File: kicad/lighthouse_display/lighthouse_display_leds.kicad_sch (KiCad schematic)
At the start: 99 parts

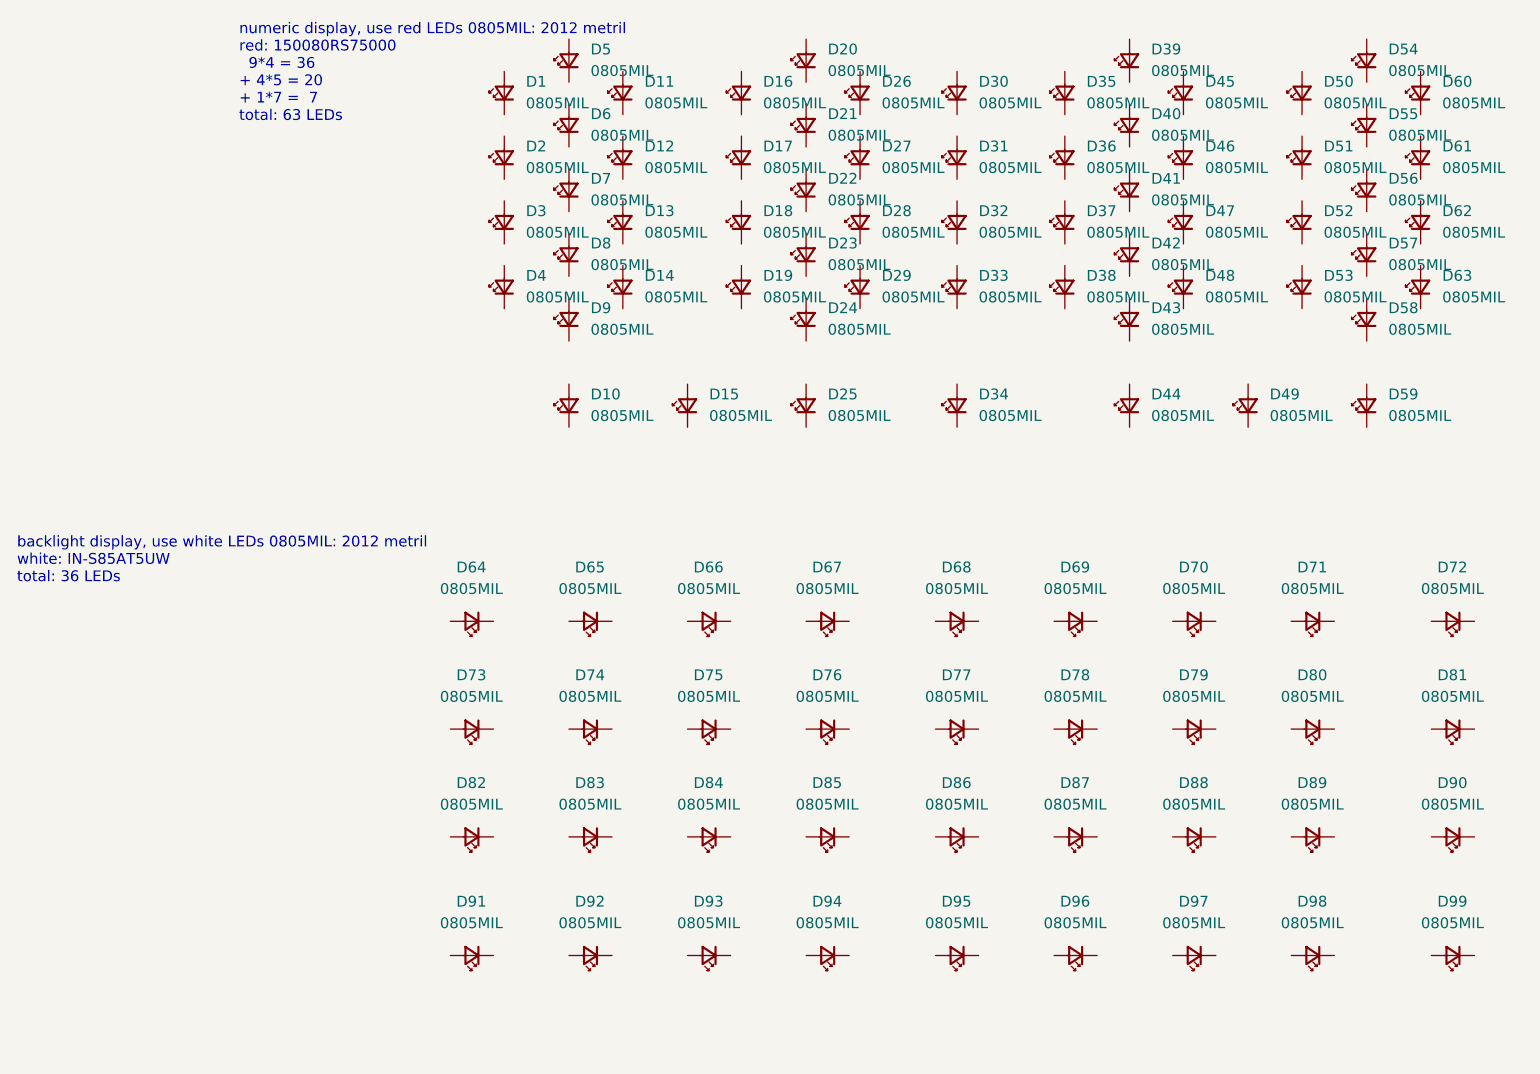
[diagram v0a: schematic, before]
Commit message: white LED driver TPS61176RTER added in lib and sch
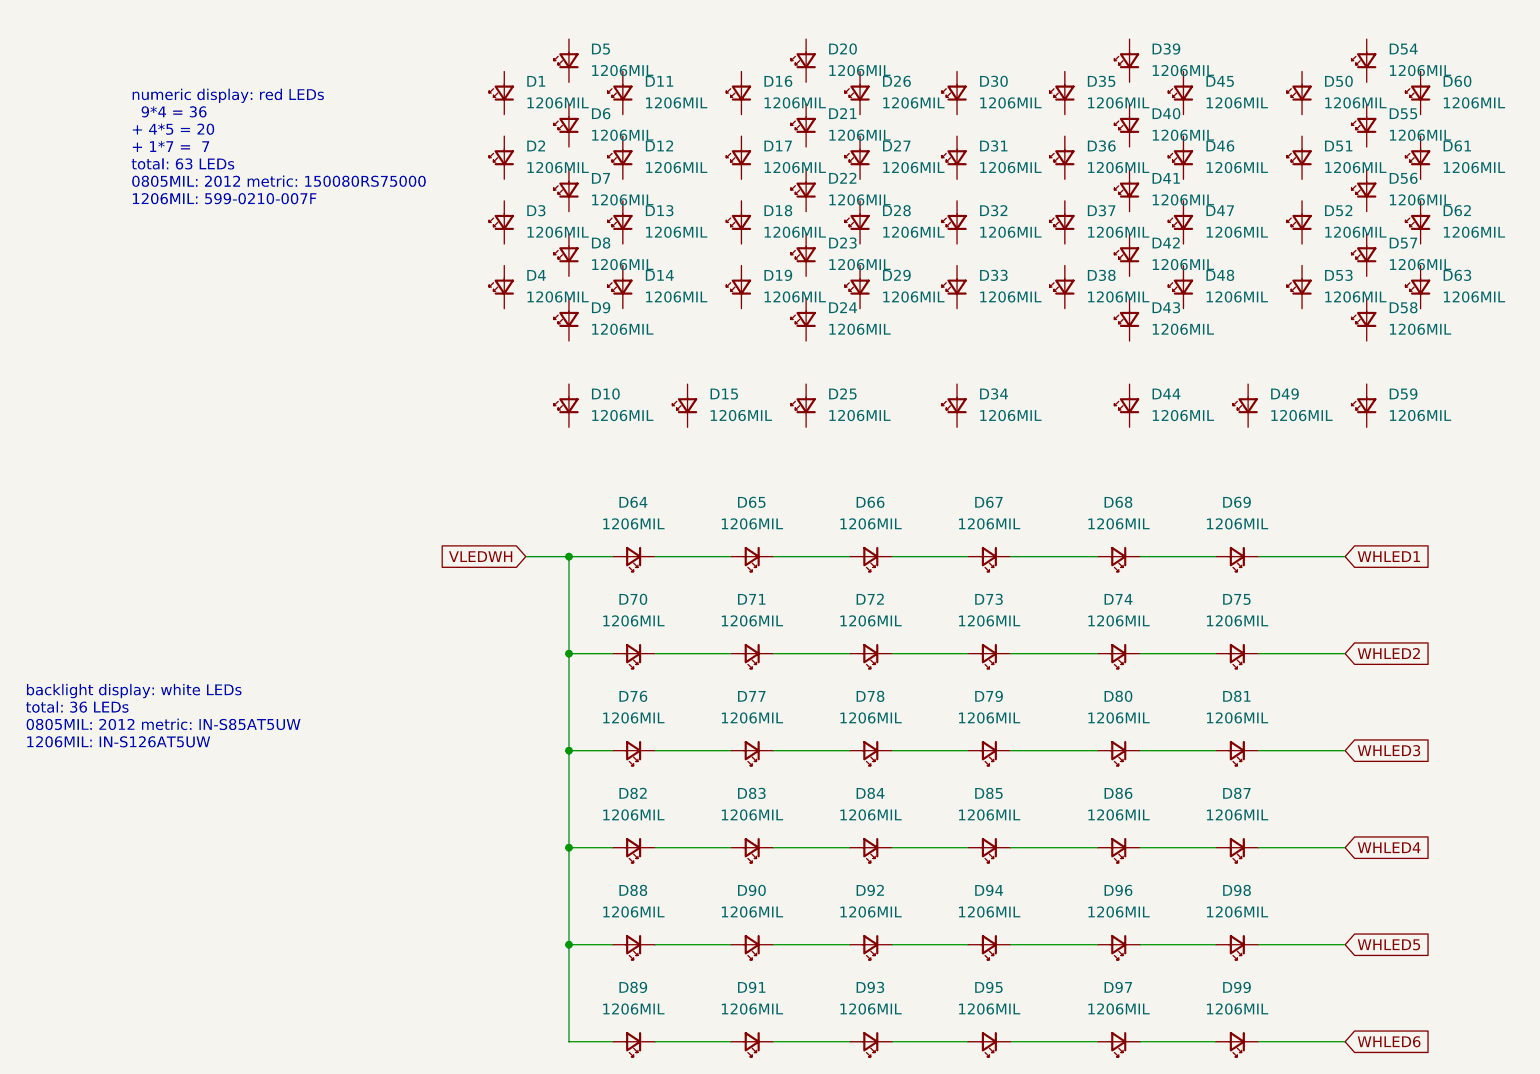
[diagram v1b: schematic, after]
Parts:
- D1, D10, D11, D12, D13, D14, D15, D16, D17, D18, D19, D2, D20, D21, D22, D23, D24, D25, D26, D27, D28, D29, D3, D30, D31, D32, D33, D34, D35, D36, D37, D38, D39, D4, D40, D41, D42, D43, D44, D45, D46, D47, D48, D49, D5, D50, D51, D52, D53, D54, D55, D56, D57, D58, D59, D6, D60, D61, D62, D63, D64, D65, D66, D67, D68, D69, D7, D70, D71, D72, D73, D74, D75, D76, D77, D78, D79, D8, D80, D81, D82, D83, D84, D85, D86, D87, D88, D89, D9, D90, D91, D92, D93, D94, D95, D96, D97, D98, D99: value 0805MIL -> 1206MIL
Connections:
- net at D84.1 (K): now also D85.2 (A)
- net at D84.2 (A): now also D83.1 (K)
- net at D76.1 (K): now also D77.2 (A)
- net VLEDWH: now reaches D76.2 (A)
- net VLEDWH: now also D64.2 (A), D70.2 (A), D82.2 (A), D88.2 (A), D89.2 (A)
- net at D79.1 (K): now also D80.2 (A)
- net at D79.2 (A): now also D78.1 (K)
- net at D80.1 (K): now also D81.2 (A)
- net at D93.1 (K): now also D95.2 (A)
- net at D93.2 (A): now also D91.1 (K)
- net at D67.1 (K): now also D68.2 (A)
- net at D67.2 (A): now also D66.1 (K)
- net at D82.1 (K): now also D83.2 (A)
- net at D97.1 (K): now also D99.2 (A)
- net at D97.2 (A): now also D95.1 (K)
- net at D91.2 (A): now also D89.1 (K)
- net WHLED6: now reaches D99.1 (K)
- net WHLED2: now reaches D75.1 (K)
- net at D75.2 (A): now also D74.1 (K)
- net at D94.1 (K): now also D96.2 (A)
- net at D94.2 (A): now also D92.1 (K)
- net at D92.2 (A): now also D90.1 (K)
- net WHLED5: now reaches D98.1 (K)
- net at D98.2 (A): now also D96.1 (K)
- net at D72.1 (K): now also D73.2 (A)
- net at D72.2 (A): now also D71.1 (K)
- net at D64.1 (K): now also D65.2 (A)
- net at D70.1 (K): now also D71.2 (A)
- net at D66.2 (A): now also D65.1 (K)
- net WHLED4: now reaches D87.1 (K)
- net at D87.2 (A): now also D86.1 (K)
- net WHLED1: now reaches D69.1 (K)
- net at D69.2 (A): now also D68.1 (K)
- net at D85.1 (K): now also D86.2 (A)
- net at D74.2 (A): now also D73.1 (K)
- net at D88.1 (K): now also D90.2 (A)
- net at D77.1 (K): now also D78.2 (A)
- net WHLED3: now reaches D81.1 (K)
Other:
- note added: "backlight display: white LEDs total: 36 LEDs 0805MIL: 2012 metric: IN-S85AT5UW 1206MIL: IN-S126AT5UW"
- note added: "numeric display: red LEDs 9*4 = 36 + 4*5 = 20 + 1*7 = 7 total: 63 LEDs 0805MIL: 2012 metric: 150080RS75000 1206MIL: 599-0210-007F"
- note removed: "backlight display, use white LEDs 0805MIL: 2012 metril white: IN-S85AT5UW total: 36 LEDs"
- note removed: "numeric display, use red LEDs 0805MIL: 2012 metril red: 150080RS75000 9*4 = 36 + 4*5 = 20 + 1*7 = 7 total: 63 LEDs"
- moved on the sheet: D64, D65, D66, D67, D68, D69

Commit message: much ado about LEDs :-)
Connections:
- net CA2: now reaches D9.1 (K)
- net CA2: now also D1.2 (A), D10.1 (K), D11.1 (K), D12.1 (K), D13.1 (K), D15.2 (A), D23.2 (A), D28.2 (A)
- net CA1: now reaches D9.2 (A)
- net CA1: now also D1.1 (K), D14.2 (A), D2.1 (K), D22.2 (A), D27.2 (A), D3.1 (K), D4.1 (K), D5.1 (K), D6.1 (K), D7.1 (K), D8.1 (K)
- net CA3: now reaches D16.1 (K)
- net CA3: now also D10.2 (A), D14.1 (K), D15.1 (K), D17.1 (K), D18.1 (K), D19.1 (K), D2.2 (A), D20.1 (K), D21.1 (K), D24.2 (A), D29.2 (A)
- net CA4: now reaches D16.2 (A)
- net CA4: now also D11.2 (A), D22.1 (K), D23.1 (K), D24.1 (K), D25.1 (K), D26.1 (K), D3.2 (A), D30.2 (A)
- net CB2: now reaches D40.1 (K)
- net CB2: now also D31.2 (A), D39.1 (K), D41.1 (K), D42.1 (K), D43.1 (K)
- net CB3: now reaches D40.2 (A)
- net CB3: now also D32.2 (A)
- net CB5: now reaches D42.2 (A)
- net CB5: now also D34.2 (A)
- net CA9: now reaches D8.2 (A)
- net CA9: now also D21.2 (A)
- net CA5: now reaches D28.1 (K)
- net CA5: now also D12.2 (A), D17.2 (A), D25.2 (A), D27.1 (K), D29.1 (K), D30.1 (K), D4.2 (A)
- net CA8: now reaches D20.2 (A)
- net CA8: now also D7.2 (A)
- net CB1: now reaches D31.1 (K)
- net CB1: now also D32.1 (K), D33.1 (K), D34.1 (K), D35.1 (K), D36.1 (K), D37.1 (K), D38.1 (K), D39.2 (A)
- net CA7: now reaches D6.2 (A)
- net CA7: now also D19.2 (A)
- net CB4: now reaches D33.2 (A)
- net CB4: now also D41.2 (A)
- net CB6: now reaches D35.2 (A)
- net CB6: now also D43.2 (A)
- net CB7: now reaches D36.2 (A)
- net CA6: now reaches D5.2 (A)
- net CA6: now also D13.2 (A), D18.2 (A), D26.2 (A)
- net CB8: now reaches D37.2 (A)
- net CB9: now reaches D38.2 (A)
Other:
- note added: "C1-1"
- note added: "C1-10"
- note added: "C1-11"
- note added: "C1-12"
- note added: "C1-13"
- note added: "C1-14"
- note added: "C1-15"
- note added: "C1-16"
- note added: "C1-2"
- note added: "C1-3"
- note added: "C1-4"
- note added: "C1-5"
- note added: "C1-6"
- note added: "C1-7"
- note added: "C1-8"
- note added: "C1-9"
- note added: "C2-1"
- note added: "C2-10"
- note added: "C2-11"
- note added: "C2-12"
- note added: "C2-13"
- note added: "C2-2"
- note added: "C2-3"
- note added: "C2-4"
- note added: "C2-5"
- note added: "C2-9"
- note added: "C3-1"
- note added: "C3-2"
- note added: "C3-3"
- note added: "C3-4"
- note added: "C3-5"
- note added: "C3-6"
- note added: "C3-7"
- note added: "C3-8"
- note added: "C4-1"
- note added: "C4-2"
- note added: "C4-3"
- note added: "C4-4"
- note added: "C4-5"
- note added: "C5-1"
- note added: "C5-2"
- note added: "C5-3"
- note added: "C5-4"
- note added: "C5-5"
- note added: "C5-6"
- note added: "C5-7"
- note added: "CA"
- note added: "CB"
- moved on the sheet: D1, D2, D3, D4, D64, D65, D66, D67, D68, D69, D70, D71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

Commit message: sch: all leds connected, also set all footprints
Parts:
- D1, D10, D11, D12, D13, D14, D15, D16, D17, D18, D19, D2, D20, D21, D22, D23, D24, D25, D26, D27, D28, D29, D3, D30, D31, D32, D33, D34, D35, D36, D37, D38, D39, D4, D40, D41, D42, D43, D44, D45, D46, D47, D48, D49, D5, D50, D51, D52, D53, D54, D55, D56, D57, D58, D59, D6, D60, D61, D62, D63, D64, D65, D66, D67, D68, D69, D7, D70, D71, D72, D73, D74, D75, D76, D77, D78, D79, D8, D80, D81, D82, D83, D84, D85, D86, D87, D88, D89, D9, D90, D91, D92, D93, D94, D95, D96, D97, D98, D99: footprint (none) -> LED_SMD:LED_1206_3216Metric_Pad1.42x1.75mm_HandSolder
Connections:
- net CB1: now also D44.2 (A), D52.2 (A), D57.2 (A)
- net CB2: now also D45.2 (A), D53.2 (A), D58.2 (A)
- net CB3: now also D44.1 (K), D45.1 (K), D46.1 (K), D47.1 (K), D48.1 (K), D49.1 (K), D50.1 (K), D51.1 (K), D54.2 (A), D59.2 (A)
- net CB4: now also D46.2 (A), D52.1 (K), D53.1 (K), D54.1 (K), D55.1 (K), D56.1 (K), D60.2 (A)
- net CB5: now also D47.2 (A), D55.2 (A), D57.1 (K), D58.1 (K), D59.1 (K), D60.1 (K), D61.1 (K), D62.1 (K), D63.1 (K)
- net CB6: now also D48.2 (A), D56.2 (A), D61.2 (A)
- net CB7: now also D49.2 (A), D62.2 (A)
- net CB8: now also D50.2 (A), D63.2 (A)
- net CB9: now also D51.2 (A)
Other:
- note added: "C3-10"
- note added: "C3-11"
- note added: "C3-12"
- note added: "C3-13"
- note added: "C3-14"
- note added: "C3-15"
- note added: "C3-16"
- note added: "C3-9"
- note added: "C4-10"
- note added: "C4-11"
- note added: "C4-12"
- note added: "C4-13"
- note added: "C4-9"
- note added: "C5-10"
- note added: "C5-11"
- note added: "C5-12"
- note added: "C5-13"
- note added: "C5-14"
- note added: "C5-15"
- note added: "C5-9"
- note removed: "C5-5"
- note removed: "C5-6"
- note removed: "C5-7"
- moved on the sheet: D1, D10, D11, D12, D13, D14, D15, D16, D17, D18, D19, D2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

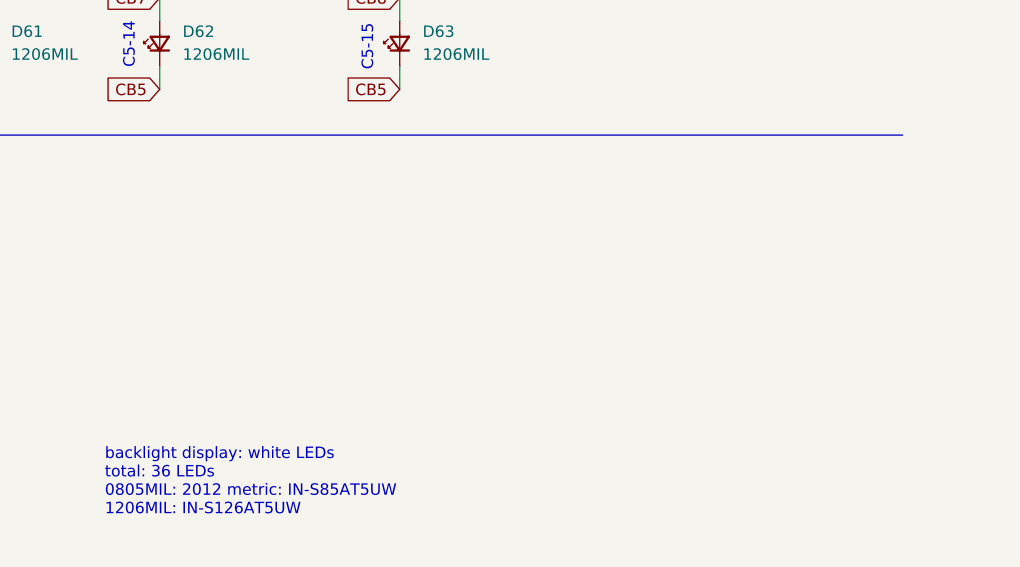
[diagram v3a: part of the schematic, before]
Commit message: places both led drivers, started routing
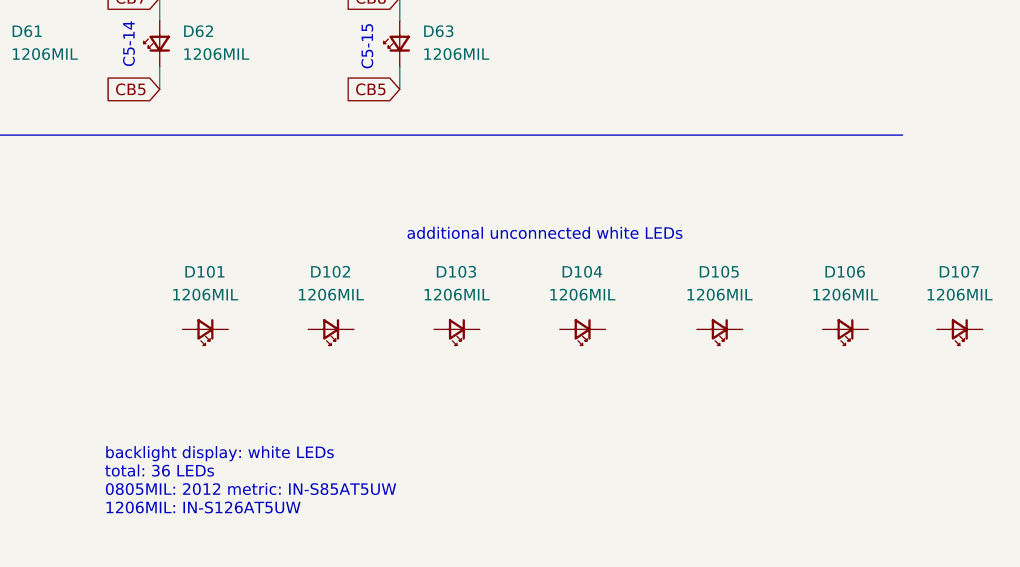
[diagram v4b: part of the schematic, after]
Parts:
- added D101, D102, D103, D104, D105, D106, D107: 1206MIL, LED_SMD:LED_1206_3216Metric_Pad1.42x1.75mm_HandSolder, symbol Device:LED_Small
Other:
- note added: "additional unconnected white LEDs"

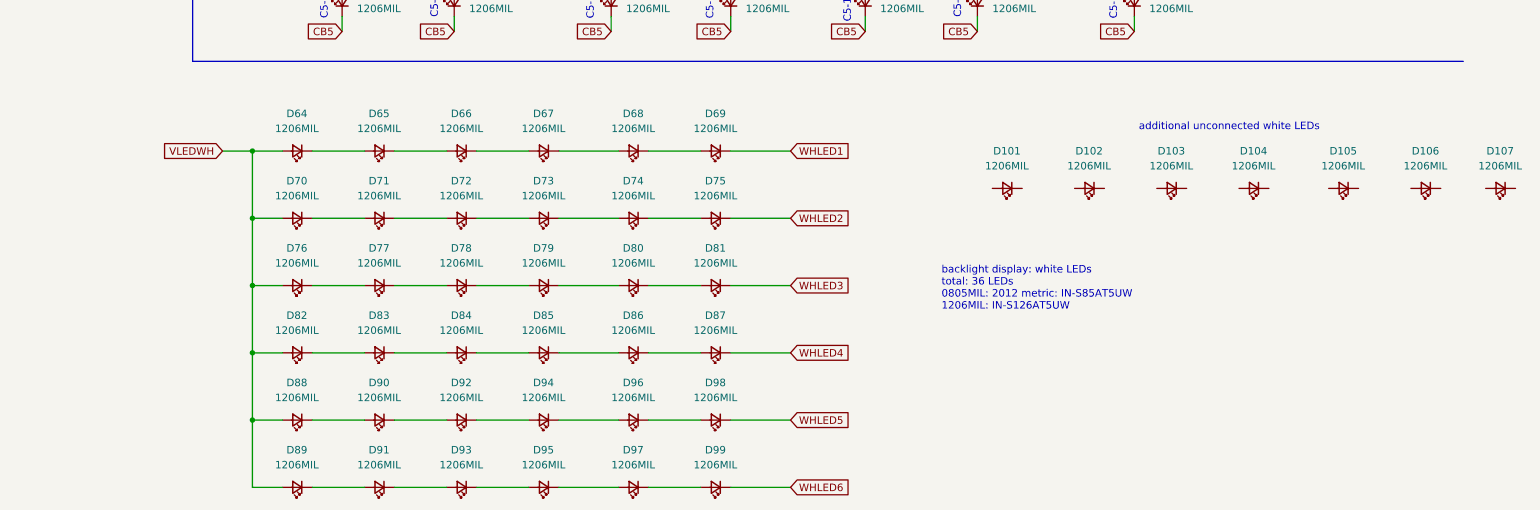
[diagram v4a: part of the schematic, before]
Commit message: use 7*6 white LEDs in a row now, almost all leds connected
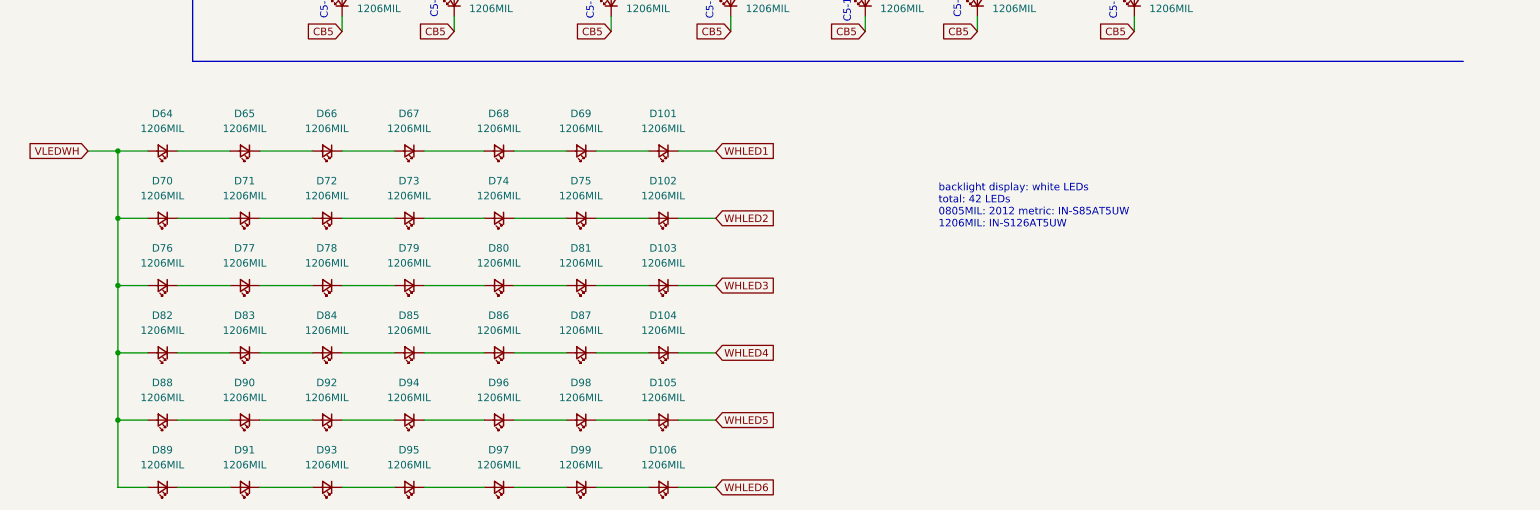
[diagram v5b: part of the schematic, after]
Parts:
- removed D107: 1206MIL, LED_SMD:LED_1206_3216Metric_Pad1.42x1.75mm_HandSolder, symbol Device:LED_Small
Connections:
- net WHLED1: now also D101.1 (K); no longer D69.1 (K)
- net WHLED2: now also D102.1 (K); no longer D75.1 (K)
- net WHLED3: now also D103.1 (K); no longer D81.1 (K)
- net WHLED4: now also D104.1 (K); no longer D87.1 (K)
- net WHLED5: now also D105.1 (K); no longer D98.1 (K)
- net WHLED6: now also D106.1 (K); no longer D99.1 (K)
- net at D105.2 (A): now also D98.1 (K)
- net at D104.2 (A): now also D87.1 (K)
- net at D106.2 (A): now also D99.1 (K)
- net at D103.2 (A): now also D81.1 (K)
- net at D102.2 (A): now also D75.1 (K)
- net at D101.2 (A): now also D69.1 (K)
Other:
- note added: "backlight display: white LEDs total: 42 LEDs 0805MIL: 2012 metric: IN-S85AT5UW 1206MIL: IN-S126AT5UW"
- note removed: "additional unconnected white LEDs"
- note removed: "backlight display: white LEDs total: 36 LEDs 0805MIL: 2012 metric: IN-S85AT5UW 1206MIL: IN-S126AT5UW"
- moved on the sheet: D101, D102, D103, D104, D105, D106, D64, D65, D66, D67, D68, D69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
